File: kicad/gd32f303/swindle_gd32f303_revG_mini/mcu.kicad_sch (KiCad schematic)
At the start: 17 parts, among them J40 J40, J7 Conn_01x05_Pin, U1 GD32F303, Y2 8Mhz

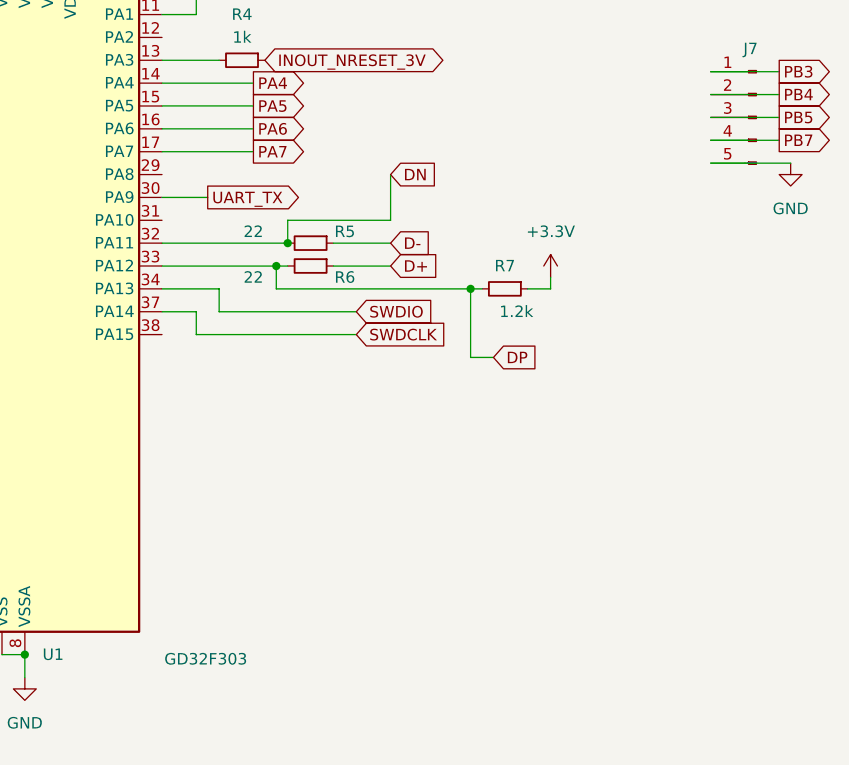
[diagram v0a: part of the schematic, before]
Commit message: add a WS2812b to the mini version, mini version for CH32,GD32 and RP2xxx
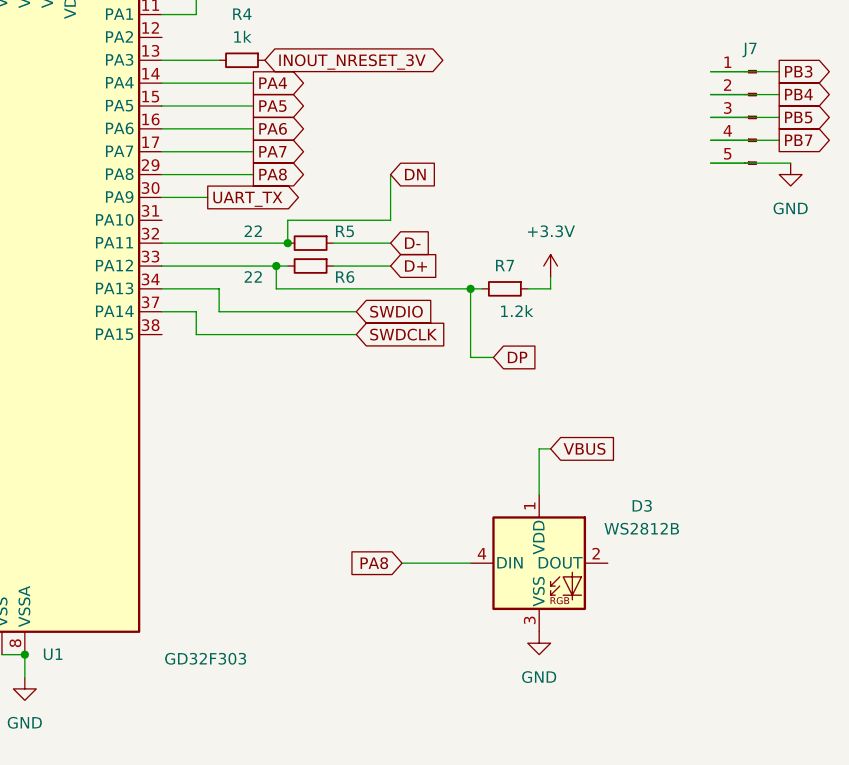
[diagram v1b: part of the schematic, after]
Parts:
- added D3: WS2812B, LED_SMD:LED_WS2812B_PLCC4_5.0x5.0mm_P3.2mm, symbol LED:WS2812B
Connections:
- net GND: now also D3.3 (VSS)
- net PA8: now reaches U1.29 (PA8)
- net PA8: now also D3.4 (DIN)
- new net VBUS: D3.1 (VDD)
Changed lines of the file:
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@@
+	(wire
+		(pts
+			(xy 198.12 115.57) (xy 196.85 115.57)
+		)
+		(stroke
+			(width 0)
+			(type default)
+		)
+	)
 	(wire
 		(pts
@@
 	(wire
 		(pts
+			(xy 154.94 85.09) (xy 165.1 85.09)
+		)
+		(stroke
+			(width 0)
+			(type default)
+		)
+	)
+	(wire
+		(pts
 			(xy 154.94 80.01) (xy 165.1 80.01)
 		)
@@
 	(wire
 		(pts
+			(xy 181.61 128.27) (xy 189.23 128.27)
+		)
+		(stroke
+			(width 0)
+			(type default)
+		)
+	)
+	(wire
+		(pts
 			(xy 96.52 81.28) (xy 99.06 81.28)
 		)
@@
 	(wire
 		(pts
+			(xy 196.85 115.57) (xy 196.85 120.65)
+		)
+		(stroke
+			(width 0)
+			(type default)
+		)
+	)
+	(wire
+		(pts
 			(xy 158.75 102.87) (xy 158.75 100.33)
 		)
@@
 			(width 0)
 			(type default)
+		)
+	)
+	(global_label "VBUS"
+		(shape input)
+		(at 198.12 115.57 0)
+		(fields_autoplaced yes)
+		(effects
+			(font
+				(size 1.27 1.27)
+			)
+			(justify left)
+		)
+		(property "Intersheetrefs" "${INTERSHEET_REFS}"
+			(at 206.0038 115.57 0)
+			(effects
+				(font
+					(size 1.27 1.27)
+				)
+				(justify left)
+				(hide yes)
+			)
 		)
 	)
@@
 		)
 	)
+	(global_label "PA8"
+		(shape input)
+		(at 181.61 128.27 180)
+		(fields_autoplaced yes)
+		(effects
+			(font
+				(size 1.27 1.27)
+			)
+			(justify right)
+		)
+		(property "Intersheetrefs" "${INTERSHEET_REFS}"
+			(at 175.0567 128.27 0)
+			(effects
+				(font
+					(size 1.27 1.27)
+				)
+				(justify right)
+				(hide yes)
+			)
+		)
+	)
 	(global_label "INOUT_NRESET_3V"
 		(shape bidirectional)
@@
 				)
 				(justify right)
+				(hide yes)
+			)
+		)
+	)
+	(global_label "PA8"
+		(shape output)
+		(at 165.1 85.09 0)
+		(fields_autoplaced yes)
+		(effects
+			(font
+				(size 1.27 1.27)
+			)
+			(justify left)
+		)
+		(property "Intersheetrefs" "${INTERSHEET_REFS}"
+			(at 171.6533 85.09 0)
+			(effects
+				(font
+					(size 1.27 1.27)
+				)
+				(justify left)
 				(hide yes)
 			)
@@
 	)
 	(symbol
+		(lib_id "power:GND")
+		(at 196.85 135.89 0)
+		(unit 1)
+		(exclude_from_sim no)
+		(in_bom yes)
+		(on_board yes)
+		(dnp no)
+		(fields_autoplaced yes)
+		(property "Reference" "#PWR01"
+			(at 196.85 142.24 0)
+			(effects
+				(font
+					(size 1.27 1.27)
+				)
+				(hide yes)
+			)
+		)
+		(property "Value" "GND"
+			(at 196.85 140.97 0)
+			(effects
+				(font
+					(size 1.27 1.27)
+				)
+			)
+		)
+		(property "Footprint" ""
+			(at 196.85 135.89 0)
+			(effects
+				(font
+					(size 1.27 1.27)
+				)
+				(hide yes)
+			)
+		)
+		(property "Datasheet" ""
+			(at 196.85 135.89 0)
+			(effects
+				(font
+					(size 1.27 1.27)
+				)
+				(hide yes)
+			)
+		)
+		(property "Description" ""
+			(at 196.85 135.89 0)
+			(effects
+				(font
+					(size 1.27 1.27)
+				)
+				(hide yes)
+			)
+		)
+		(pin "1"
+		)
+		(instances
+			(project "gd32f303_revG_mini"
+				(path "/fbe443d6-6d74-4abc-9dee-16e0160553bc/860eb7d0-1eba-4c3d-ac2c-5a3607b90fb5"
+					(reference "#PWR01")
+					(unit 1)
+				)
+			)
+		)
+	)
+	(symbol
 		(lib_id "Device:Crystal_GND24")
 		(at 104.14 81.28 270)
@@
 					(unit 1)
 				)
+			)
+		)
+	)
+	(symbol
+		(lib_id "LED:WS2812B")
+		(at 196.85 128.27 0)
+		(unit 1)
+		(exclude_from_sim no)
+		(in_bom yes)
+		(on_board yes)
+		(dnp no)
+		(fields_autoplaced yes)
+		(property "Reference" "D3"
+			(at 208.28 121.9514 0)
+			(effects
+				(font
+					(size 1.27 1.27)
+				)
+			)
+		)
+		(property "Value" "WS2812B"
+			(at 208.28 124.4914 0)
+			(effects
+				(font
+					(size 1.27 1.27)
+				)
+			)
+		)
+		(property "Footprint" "LED_SMD:LED_WS2812B_PLCC4_5.0x5.0mm_P3.2mm"
+			(at 198.12 135.89 0)
+			(effects
+				(font
+					(size 1.27 1.27)
+				)
+				(justify left top)
+				(hide yes)
+			)
+		)
+		(property "Datasheet" "https://cdn-shop.adafruit.com/datasheets/WS2812B.pdf"
+			(at 199.39 137.795 0)
+			(effects
+				(font
+					(size 1.27 1.27)
+				)
+				(justify left top)
+				(hide yes)
+			)
+		)
+		(property "Description" "RGB LED with integrated controller"
+			(at 196.85 128.27 0)
+			(effects
+				(font
+					(size 1.27 1.27)
+				)
+				(hide yes)
+			)
+		)
+		(pin "2"
+		)
+		(pin "1"
+		)
+		(pin "4"
+		)
+		(pin "3"
+		)
+		(instances
+			(project ""
+				(path "/fbe443d6-6d74-4abc-9dee-16e0160553bc/860eb7d0-1eba-4c3d-ac2c-5a3607b90fb5"
+					(reference "D3")
+					(unit 1)
+				)

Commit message: kicad: order to pcbway
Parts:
- added C1: 100n, Resistor_SMD:R_0603_1608Metric, symbol Device:C_Small
- added Q1: DMG2302U, Package_TO_SOT_SMD:SOT-23, symbol Transistor_FET:DMG2302U
- added R1: 1k, Resistor_SMD:R_0603_1608Metric, symbol Device:R_Small
- added R11: 330, Resistor_SMD:R_0603_1608Metric, symbol Device:R_Small
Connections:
- net GND: now also C1.2, Q1.2 (S), R1.2
- net INOUT_NRESET_3V: no longer U1.42 (PB6)
- net PA8: no longer D3.4 (DIN)
- net PB4: now also D3.4 (DIN)
- net VBUS: now also C1.1
- new net: Q1.3 (D), R11.2
- new net DRIVE_RESET: Q1.1 (G), R1.1, U1.42 (PB6)
- new net INOUT_NRESET: R11.1

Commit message: kicad, gd32 mini: add back the boot0 pulldown (duh)
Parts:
- added R12: 10k, Resistor_SMD:R_0603_1608Metric, symbol Device:R_Small
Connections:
- net GND: now also R12.2
- net at U1.20 (PB2), U1.44 (BOOT0): now also R12.1
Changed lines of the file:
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@@
 	)
 	(junction
+		(at 72.39 74.93)
+		(diameter 0)
+		(color 0 0 0 0)
+	)
+	(junction
 		(at 142.24 59.69)
 		(diameter 0)
@@
 	)
 	(junction
+		(at 78.74 69.85)
+		(diameter 0)
+		(color 0 0 0 0)
+	)
+	(junction
 		(at 189.23 97.79)
 		(diameter 0)
@@
 	(wire
 		(pts
+			(xy 78.74 69.85) (xy 78.74 97.79)
+		)
+		(stroke
+			(width 0)
+			(type default)
+		)
+	)
+	(wire
+		(pts
+			(xy 121.92 97.79) (xy 78.74 97.79)
+		)
+		(stroke
+			(width 0)
+			(type default)
+		)
+	)
+	(wire
+		(pts
 			(xy 154.94 77.47) (xy 165.1 77.47)
 		)
@@
 	(wire
 		(pts
-			(xy 83.82 69.85) (xy 83.82 97.79)
-		)
-		(stroke
-			(width 0)
-			(type default)
-		)
-	)
-	(wire
-		(pts
 			(xy 195.58 97.79) (xy 198.12 97.79)
 		)
@@
 	(wire
 		(pts
-			(xy 83.82 97.79) (xy 121.92 97.79)
-		)
-		(stroke
-			(width 0)
-			(type default)
-		)
-	)
-	(wire
-		(pts
 			(xy 154.94 92.71) (xy 168.91 92.71)
 		)
@@
 	(wire
 		(pts
+			(xy 72.39 74.93) (xy 72.39 76.2)
+		)
+		(stroke
+			(width 0)
+			(type default)
+		)
+	)
+	(wire
+		(pts
 			(xy 154.94 85.09) (xy 165.1 85.09)
 		)
@@
 	(wire
 		(pts
-			(xy 90.17 88.9) (xy 91.44 88.9)
+			(xy 78.74 69.85) (xy 121.92 69.85)
 		)
 		(stroke
@@
 	(wire
 		(pts
-			(xy 139.7 138.43) (xy 139.7 140.97)
+			(xy 90.17 88.9) (xy 91.44 88.9)
 		)
 		(stroke
@@
 	(wire
 		(pts
-			(xy 83.82 69.85) (xy 121.92 69.85)
+			(xy 139.7 138.43) (xy 139.7 140.97)
 		)
 		(stroke
@@
 	(wire
 		(pts
+			(xy 72.39 69.85) (xy 78.74 69.85)
+		)
+		(stroke
+			(width 0)
+			(type default)
+		)
+	)
+	(wire
+		(pts
 			(xy 77.47 125.73) (xy 81.28 125.73)
 		)
@@
 	)
 	(symbol
+		(lib_id "power:GND")
+		(at 72.39 74.93 0)
+		(unit 1)
+		(exclude_from_sim no)
+		(in_bom yes)
+		(on_board yes)
+		(dnp no)
+		(fields_autoplaced yes)
+		(property "Reference" "#PWR07"
+			(at 72.39 81.28 0)
+			(effects
+				(font
+					(size 1.27 1.27)
+				)
+				(hide yes)
+			)
+		)
+		(property "Value" "GND"
+			(at 72.39 80.01 0)
+			(effects
+				(font
+					(size 1.27 1.27)
+				)
+			)
+		)
+		(property "Footprint" ""
+			(at 72.39 74.93 0)
+			(effects
+				(font
+					(size 1.27 1.27)
+				)
+				(hide yes)
+			)
+		)
+		(property "Datasheet" ""
+			(at 72.39 74.93 0)
+			(effects
+				(font
+					(size 1.27 1.27)
+				)
+				(hide yes)
+			)
+		)
+		(property "Description" ""
+			(at 72.39 74.93 0)
+			(effects
+				(font
+					(size 1.27 1.27)
+				)
+				(hide yes)
+			)
+		)
+		(pin "1"
+		)
+		(instances
+			(project "gd32f303_revG_mini"
+				(path "/fbe443d6-6d74-4abc-9dee-16e0160553bc/860eb7d0-1eba-4c3d-ac2c-5a3607b90fb5"
+					(reference "#PWR07")
+					(unit 1)
+				)
+			)
+		)
+	)
+	(symbol
 		(lib_id "Device:Crystal_GND24")
 		(at 104.14 81.28 270)
@@
 					(unit 1)
 				)
+			)
+		)
+	)
+	(symbol
+		(lib_id "Device:R_Small")
+		(at 72.39 72.39 0)
+		(unit 1)
+		(exclude_from_sim no)
+		(in_bom yes)
+		(on_board yes)
+		(dnp no)
+		(fields_autoplaced yes)
+		(property "Reference" "R12"
+			(at 74.93 71.12 0)
+			(effects
+				(font
+					(size 1.27 1.27)
+				)
+				(justify left)
+			)
+		)
+		(property "Value" "10k"
+			(at 74.93 73.66 0)
+			(effects
+				(font
+					(size 1.27 1.27)
+				)
+				(justify left)
+			)
+		)
+		(property "Footprint" "Resistor_SMD:R_0603_1608Metric"
+			(at 72.39 72.39 0)
+			(effects
+				(font
+					(size 1.27 1.27)
+				)
+				(hide yes)
+			)
+		)
+		(property "Datasheet" "~"
+			(at 72.39 72.39 0)
+			(effects
+				(font
+					(size 1.27 1.27)
+				)
+				(hide yes)
+			)
+		)
+		(property "Description" ""
+			(at 72.39 72.39 0)
+			(effects
+				(font
+					(size 1.27 1.27)
+				)
+				(hide yes)
+			)
+		)
+		(pin "1"
+		)
+		(pin "2"
+		)
+		(instances
+			(project "gd32f303_revG_mini"
+				(path "/fbe443d6-6d74-4abc-9dee-16e0160553bc/860eb7d0-1eba-4c3d-ac2c-5a3607b90fb5"
+					(reference "R12")
+					(unit 1)
+				)
